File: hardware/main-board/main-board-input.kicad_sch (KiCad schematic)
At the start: 36 parts, among them J4 Conn_01x02, SW1 SW_Push_Long, SW10 SW_Push_LED, SW11 Rotary_Encoder_Switch, SW2 SW_Push_Long, SW3 SW_Push, SW4 SW_Push, SW5 SW_Push, SW6 SW_Push, SW7 SW_Push_LED, SW8 SW_Push_LED, SW9 SW_Push_LED, U7 TCA8418, U8 STP16CPC26

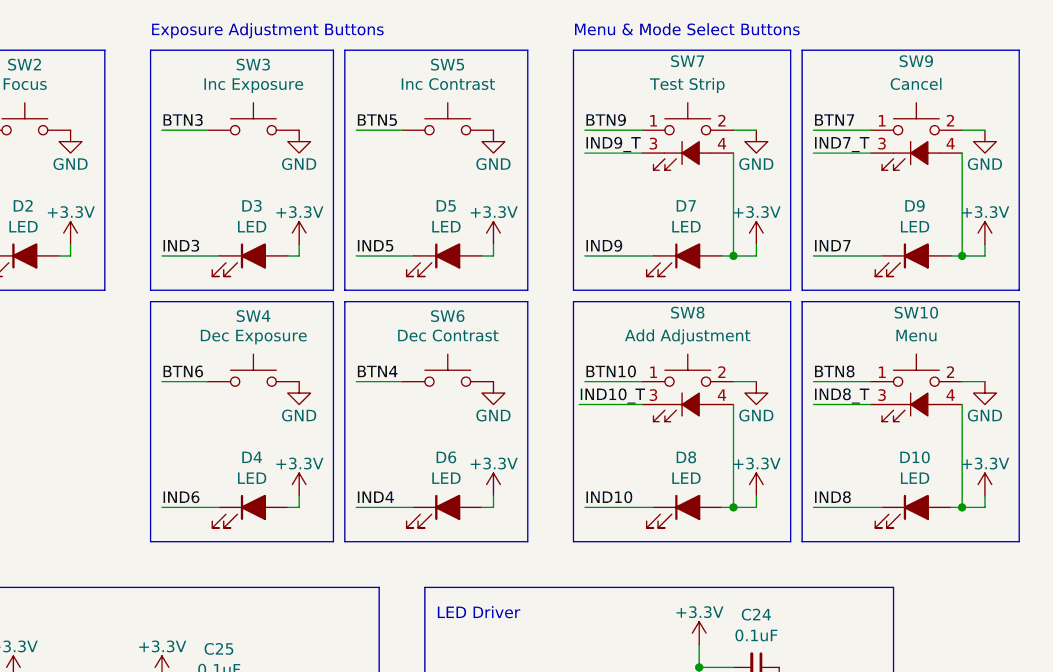
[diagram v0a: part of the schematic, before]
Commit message: Fixed some label mishaps from the previous update
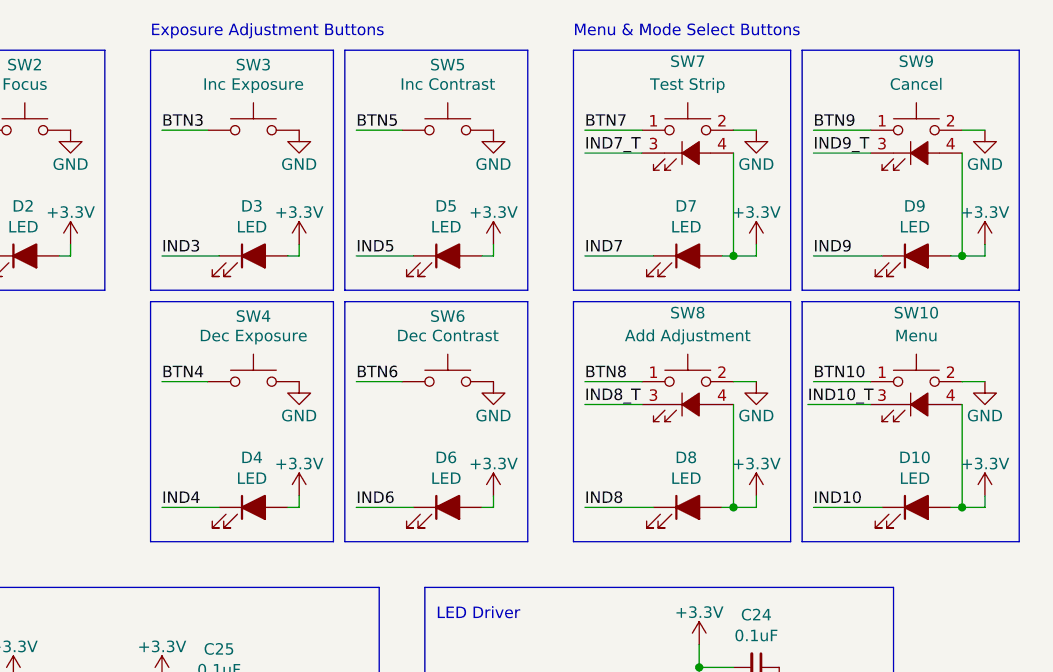
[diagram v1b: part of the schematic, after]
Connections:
- net BTN10: now also SW10.1; no longer SW8.1
- net BTN4: now also SW4.1; no longer SW6.1
- net BTN6: now also SW6.1; no longer SW4.1
- net BTN7: now also SW7.1; no longer SW9.1
- net BTN8: now also SW8.1; no longer SW10.1
- net BTN9: now also SW9.1; no longer SW7.1
- net IND10: now also D10.1 (K); no longer D8.1 (K)
- net IND10_T: now also SW10.3 (K); no longer SW8.3 (K)
- net IND4: now also D4.1 (K); no longer D6.1 (K)
- net IND6: now also D6.1 (K); no longer D4.1 (K)
- net IND7: now also D7.1 (K); no longer D9.1 (K)
- net IND7_T: now also SW7.3 (K); no longer SW9.3 (K)
- net IND8: now also D8.1 (K); no longer D10.1 (K)
- net IND8_T: now also SW8.3 (K); no longer SW10.3 (K)
- net IND9: now also D9.1 (K); no longer D7.1 (K)
- net IND9_T: now also SW9.3 (K); no longer SW7.3 (K)

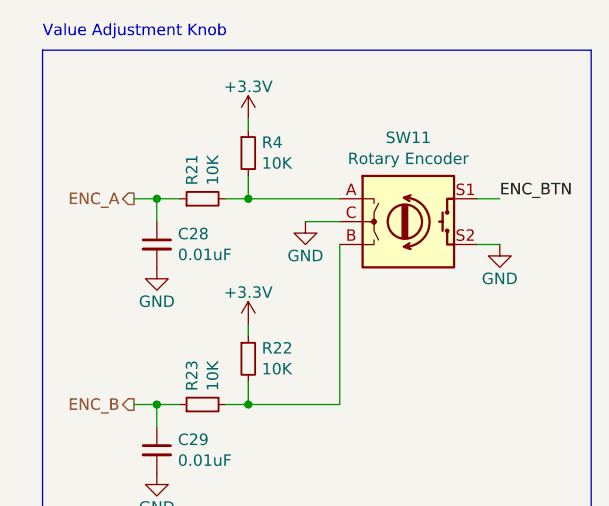
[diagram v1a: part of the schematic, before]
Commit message: Update main board to KiCad v7
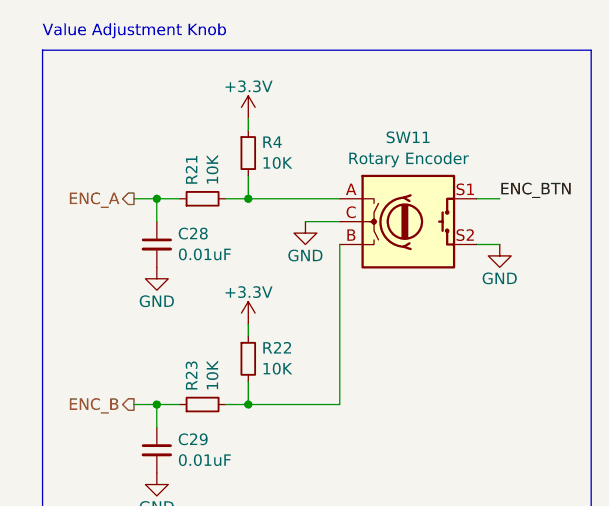
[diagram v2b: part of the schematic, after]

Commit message: Change LED driver IC based on availability
This is just a part variant and footprint change, only schematic updates
are in the metadata.
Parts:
- U8: footprint Package_SO:TSSOP-24_4.4x7.8mm_P0.65mm -> Package_SO:QSOP-24_3.9x8.7mm_P0.635mm; Manufacturer PN STP16CPC26TTR -> STP16CPC26PTR; Supplier PN 497-11985-1-ND -> 497-11923-1-ND
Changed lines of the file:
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@@
       (effects (font (size 1.27 1.27)))
     )
-    (property "Footprint" "Package_SO:TSSOP-24_4.4x7.8mm_P0.65mm" (at 125.73 118.11 0)
+    (property "Footprint" "Package_SO:QSOP-24_3.9x8.7mm_P0.635mm" (at 125.73 118.11 0)
       (effects (font (size 1.27 1.27)) hide)
     )
@@
       (effects (font (size 1.27 1.27)) hide)
     )
-    (property "Description" "IC LED DRVR LIN DIM 90MA 24TSSOP" (at 125.73 118.11 0)
+    (property "Description" "IC LED DRVR LIN DIM 90MA 24QSOP" (at 125.73 118.11 0)
       (effects (font (size 1.27 1.27)) hide)
     )
@@
       (effects (font (size 1.27 1.27)) hide)
     )
-    (property "Manufacturer PN" "STP16CPC26TTR" (at 125.73 118.11 0)
+    (property "Manufacturer PN" "STP16CPC26PTR" (at 125.73 118.11 0)
       (effects (font (size 1.27 1.27)) hide)
     )
@@
       (effects (font (size 1.27 1.27)) hide)
     )
-    (property "Supplier PN" "497-11985-1-ND" (at 125.73 118.11 0)
+    (property "Supplier PN" "497-11923-1-ND" (at 125.73 118.11 0)
       (effects (font (size 1.27 1.27)) hide)
     )

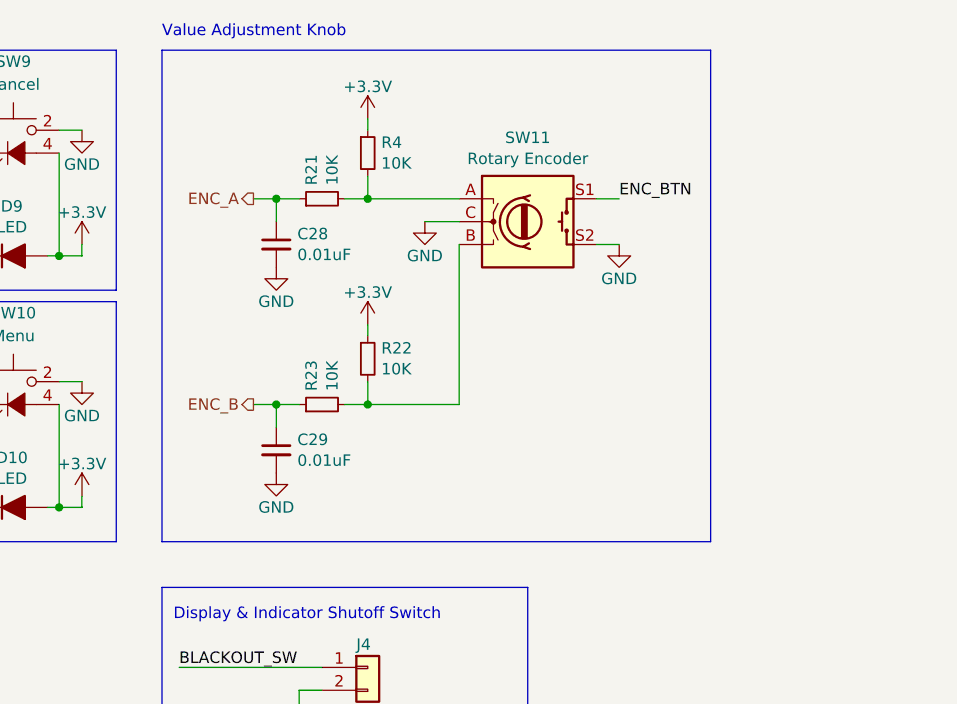
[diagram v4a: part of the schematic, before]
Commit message: Updated TVS diodes for certain input components
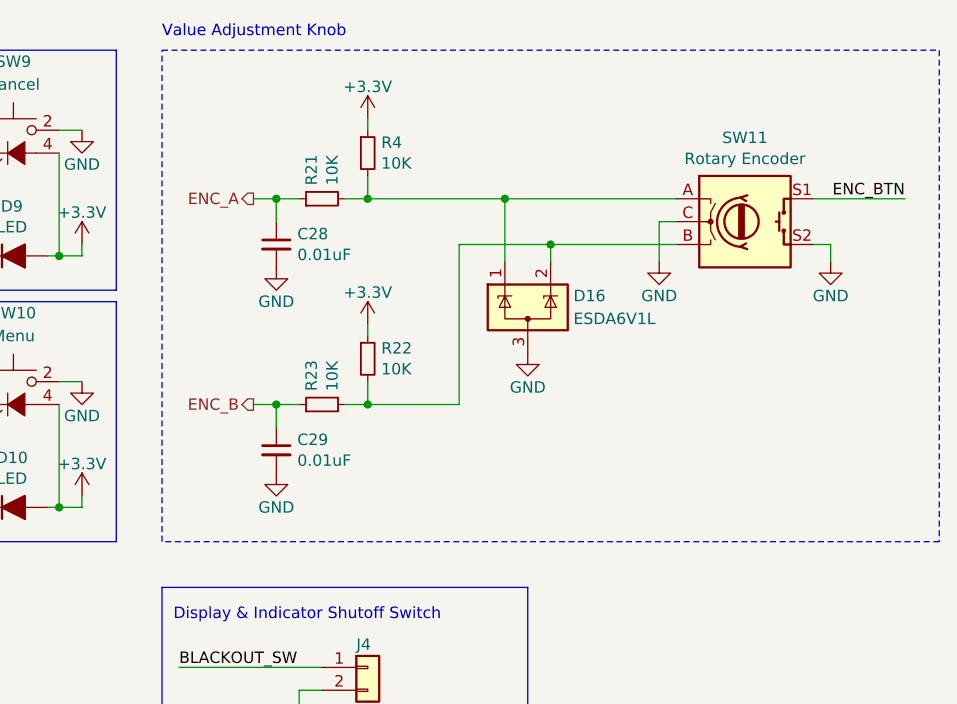
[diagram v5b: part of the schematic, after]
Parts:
- added D16: ESDA6V1L, lib_fp:SOT23-3L, symbol Project:ESDA6V1L
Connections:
- net GND: now also D16.3 (A)
- net at R21.2, R4.2, SW11.A: now also D16.1 (K)
- net at R22.2, R23.2, SW11.B: now also D16.2 (K)
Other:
- moved on the sheet: SW11

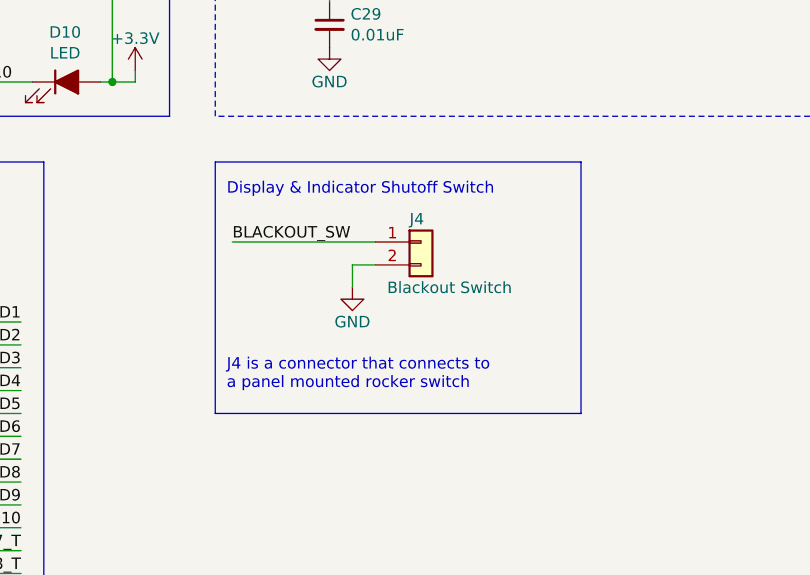
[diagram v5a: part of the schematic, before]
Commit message: Changed blackout switch connector from THT to SMD
This is an internal connector, which does not experience any mechanical
stress. Should just stich with SMD for ease of assembly.
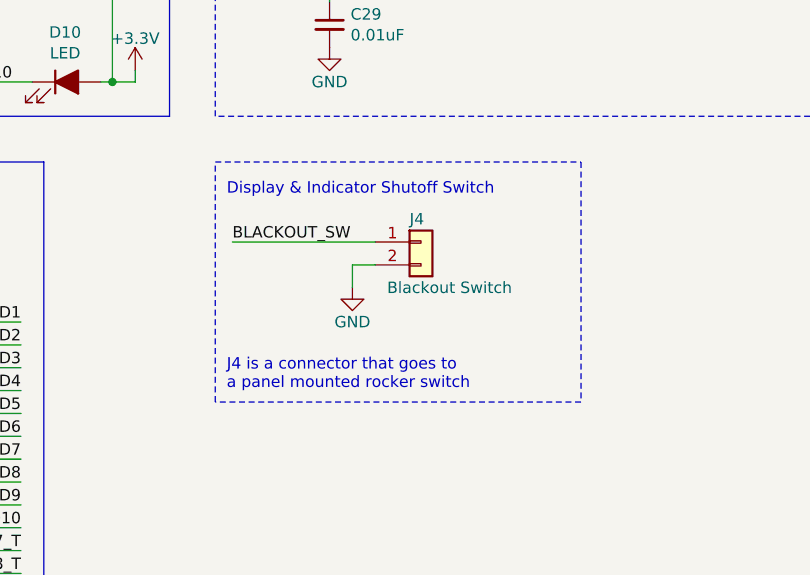
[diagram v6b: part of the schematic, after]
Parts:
- J4: footprint Connector_JST:JST_PH_B2B-PH-K_1x02_P2.00mm_Vertical -> Connector_JST:JST_PH_B2B-PH-SM4-TB_1x02-1MP_P2.00mm_Vertical; Manufacturer PN B2B-PH-K-S(LF)(SN) -> B2B-PH-SM4-TB(LF)(SN); Supplier Digi-Key -> Newark; Supplier PN 455-1704-ND -> 37K9941
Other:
- note added: "J4 is a connector that goes to a panel mounted rocker switch"
- note removed: "J4 is a connector that connects to a panel mounted rocker switch"
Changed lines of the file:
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@@
-    (stroke (width 0) (type default))
-  )
-  (polyline (pts (xy 166.37 105.41) (xy 207.01 105.41))
     (stroke (width 0) (type default))
   )
@@
     (stroke (width 0) (type default))
   )
-  (polyline (pts (xy 207.01 77.47) (xy 166.37 77.47))
-    (stroke (width 0) (type default))
-  )
   (wire (pts (xy 106.68 95.25) (xy 115.57 95.25))
     (stroke (width 0) (type default))
@@
     (stroke (width 0) (type default))
   )
-  (polyline (pts (xy 166.37 77.47) (xy 166.37 105.41))
-    (stroke (width 0) (type default))
-  )
   (polyline (pts (xy 147.32 77.47) (xy 95.25 77.47))
     (stroke (width 0) (type default))
@@
   )
   (wire (pts (xy 78.74 110.49) (xy 86.36 110.49))
-    (stroke (width 0) (type default))
-  )
-  (polyline (pts (xy 207.01 105.41) (xy 207.01 77.47))
     (stroke (width 0) (type default))
   )
@@
     (fill (type none))
   )
+  (rectangle (start 166.37 77.47) (end 207.01 104.14)
+    (stroke (width 0) (type dash))
+    (fill (type none))
+  )
   (text "Menu & Mode Select Buttons" (at 111.76 16.51 0)
     (effects (font (size 1.27 1.27)) (justify left bottom))
@@
     (effects (font (size 1.27 1.27)) (justify left bottom))
   )
-  (text "J4 is a connector that connects to\na panel mounted rocker switch"
+  (text "J4 is a connector that goes to\na panel mounted rocker switch"
     (at 167.64 102.87 0)
     (effects (font (size 1.27 1.27)) (justify left bottom))
@@
       (effects (font (size 1.27 1.27)) (justify left) hide)
     )
-    (property "Footprint" "Connector_JST:JST_PH_B2B-PH-K_1x02_P2.00mm_Vertical" (at 189.23 86.36 0)
-      (effects (font (size 1.27 1.27)) hide)
-    )
-    (property "Datasheet" "http://www.jst-mfg.com/product/pdf/eng/ePH.pdf" (at 189.23 86.36 0)
+    (property "Footprint" "Connector_JST:JST_PH_B2B-PH-SM4-TB_1x02-1MP_P2.00mm_Vertical" (at 189.23 86.36 0)
+      (effects (font (size 1.27 1.27)) hide)
+    )
+    (property "Datasheet" "https://www.jst-mfg.com/product/pdf/eng/ePH.pdf" (at 189.23 86.36 0)
       (effects (font (size 1.27 1.27)) hide)
     )
@@
       (effects (font (size 1.27 1.27)) hide)
     )
-    (property "Manufacturer PN" "B2B-PH-K-S(LF)(SN)" (at 189.23 86.36 0)
-      (effects (font (size 1.27 1.27)) hide)
-    )
-    (property "Supplier" "Digi-Key" (at 189.23 86.36 0)
-      (effects (font (size 1.27 1.27)) hide)
-    )
-    (property "Supplier PN" "455-1704-ND" (at 189.23 86.36 0)
-      (effects (font (size 1.27 1.27)) hide)
-    )
+    (property "Manufacturer PN" "B2B-PH-SM4-TB(LF)(SN)" (at 189.23 86.36 0)
+      (effects (font (size 1.27 1.27)) hide)
+    )
+    (property "Supplier" "Newark" (at 189.23 86.36 0)
+      (effects (font (size 1.27 1.27)) hide)
+    )
+    (property "Supplier PN" "37K9941" (at 189.23 86.36 0)
+      (effects (font (size 1.27 1.27)) hide)
+    )

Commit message: Completely reroute the main board
There may still be a lot of tweaks and changes, but the first pass of
rerouting is finished and in a good place for the time being.

Locations of connectors and other mechanical components should hopefully
be final enough for the time being.
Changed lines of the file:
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@@
   (junction (at 154.94 68.58) (diameter 0) (color 0 0 0 0)
   )
-  (no_connect (at 142.24 130.81))
+  (no_connect (at 135.89 130.81))
   (no_connect (at 135.89 133.35))
   (no_connect (at 135.89 138.43))
@@
     (stroke (width 0) (type default))
   )
-  (wire (pts (xy 142.24 130.81) (xy 135.89 130.81))
-    (stroke (width 0) (type default))
-  )

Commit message: Change panel illumination LEDs
This changes from a single LED for each spot, to a combination of LED
and spacer.  The purpose of this change is to get a little bit less
height on the LEDs, while keeping the same overall specs, for better
enclosure fit.

The specific components are:
LED: SunLED XLUR11D
Spacer: Bivar ELM 2-120
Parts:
- D1, D10, D2, D3, D4, D5, D6, D7, D8, D9: footprint LED_THT:LED_D5.0mm -> lib_fp:LED_D3.0mm_XLUR11D_ELM-2-120; Manufacturer Lite-On Inc. -> SunLED; Manufacturer PN LTL-4223 -> XLUR11D; Supplier PN 160-1127-ND -> 1497-1030-ND
